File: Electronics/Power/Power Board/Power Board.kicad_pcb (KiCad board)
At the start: 2 copper layers, 117 parts, among them IC201 INA219AIDR, IC202 INA219AIDR, IC203 MP28167GQ-A-Z, IC204 TPS563202DRLR, IC206 TPS563202DRLR, IC301 STM32U575VGT6, IC302 TJA1057GT/3, J201 Conn_01x02_Pin, J202 XT60PW-M, J203 Screw_Terminal_01x02, J204 Screw_Terminal_01x02, J205 Conn_01x02_Pin, J206 Screw_Terminal_01x02, J207 Screw_Terminal_01x02, J208 Conn_01x02_Pin, J209 XT60PW-F, J210 Screw_Terminal_01x02, J211 Screw_Terminal_01x02, J212 Conn_01x02_Pin, J301 TC2030, J302 TYPE-C-31-M-12, J303 Screw_Terminal_01x03, SW201 SW_SPDT, SW301 SW_DIP_x02, U301 USBLC6-4SC6-ES, U302 USBLC6-4SC6-ES, X301 25MHz_Clock, X302 32.768kHz_Clock

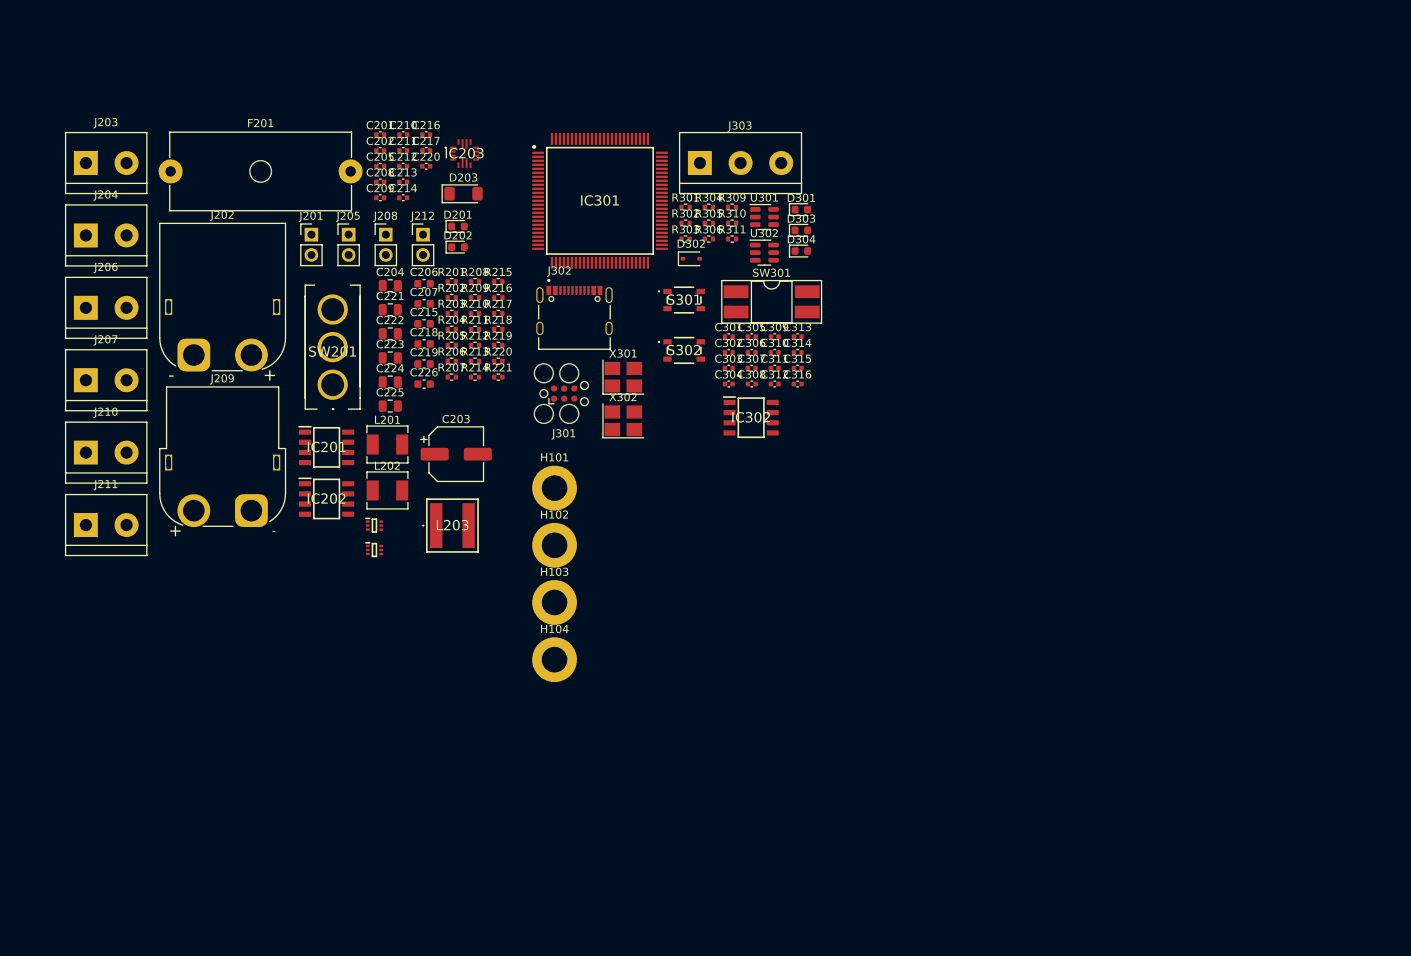
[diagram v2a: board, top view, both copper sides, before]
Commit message: Implemented power supply selector
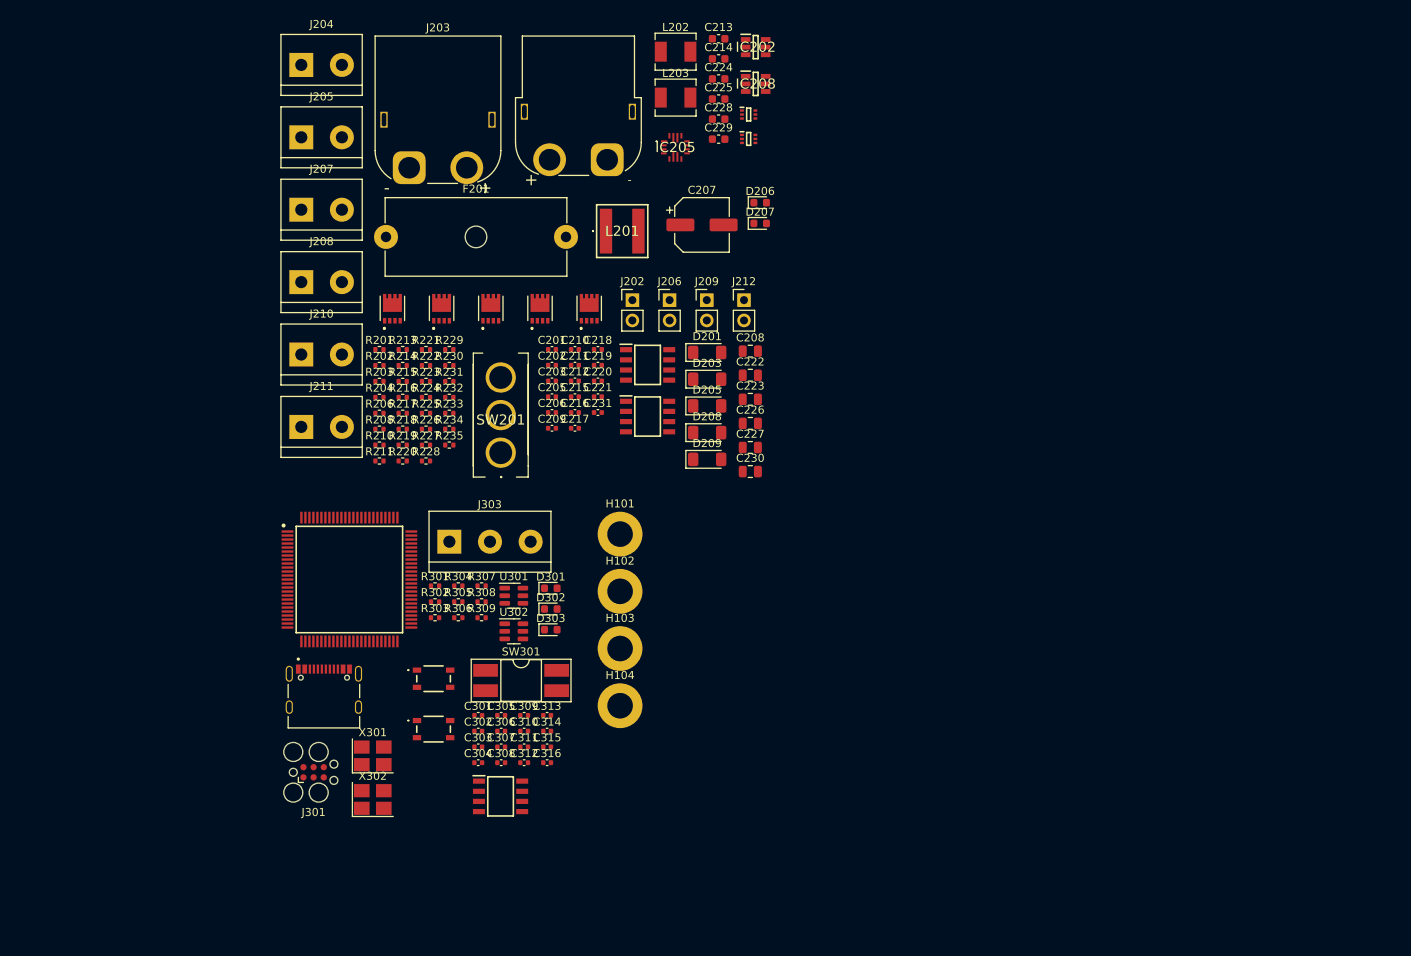
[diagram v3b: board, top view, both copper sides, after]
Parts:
- removed C204: 22u, Capacitor_SMD:C_0805_2012Metric
- removed D202: GREEN, LED_SMD:LED_0603_1608Metric
- removed D304: Blue, LED_SMD:LED_0603_1608Metric
- removed IC203: MP28167GQ-A-Z, MSL Footprints:MP28167GQAZ
- removed R205: 10m, Resistor_SMD:R_0402_1005Metric
- removed R207: 10k, Resistor_SMD:R_0402_1005Metric
- removed R209: 21k5, Resistor_SMD:R_0402_1005Metric
- removed R212: 0R, Resistor_SMD:R_0402_1005Metric
- removed R310, R311: 1k5, Resistor_SMD:R_0402_1005Metric
- added C227: 22u, Capacitor_SMD:C_0805_2012Metric, F.Cu at (194.1, 92.0)
- added C228: 22u, Capacitor_SMD:C_0603_1608Metric, F.Cu at (190.1, 50.9)
- added C229: 22u, Capacitor_SMD:C_0603_1608Metric, F.Cu at (190.1, 53.5)
- added C230: 22u, Capacitor_SMD:C_0805_2012Metric, F.Cu at (194.1, 95.0)
- added C231: 1u, Capacitor_SMD:C_0402_1005Metric, F.Cu at (175.0, 87.6)
- added D205: ZMM10V, Diode_SMD:D_MiniMELF, F.Cu at (188.7, 86.8)
- added D206: GREEN, LED_SMD:LED_0603_1608Metric, F.Cu at (195.3, 61.4)
- added D207: GREEN, LED_SMD:LED_0603_1608Metric, F.Cu at (195.3, 64.0)
- added D208: ZMM16V, Diode_SMD:D_MiniMELF, F.Cu at (188.7, 90.1)
- added D209: ZMM4V7, Diode_SMD:D_MiniMELF, F.Cu at (188.7, 93.5)
- added IC205: MP28167GQ-A-Z, MSL Footprints:MP28167GQAZ, F.Cu at (184.7, 54.5)
- added IC207: TPS563202DRLR, MSL Footprints:SOTFL50P160X60-6N, F.Cu at (193.8, 53.4)
- added IC208: TLV1805DBVR, MSL Footprints:SOT95P280X145-6N, F.Cu at (194.7, 46.5)
- added Q201: DMP3013SFV-7, MSL Footprints:DMP3013SFV7, F.Cu at (149.3, 76.1)
- added Q202: DMP3013SFV-7, MSL Footprints:DMP3013SFV7, F.Cu at (155.5, 76.1)
- added Q203: DMP3013SFV-7, MSL Footprints:DMP3013SFV7, F.Cu at (161.6, 76.1)
- added Q204: DMP3013SFV-7, MSL Footprints:DMP3013SFV7, F.Cu at (167.8, 76.1)
- added Q205: DMP3013SFV-7, MSL Footprints:DMP3013SFV7, F.Cu at (173.9, 76.1)
- added R222: 430k, Resistor_SMD:R_0402_1005Metric, F.Cu at (153.5, 81.7)
- added R223: 39k2, Resistor_SMD:R_0402_1005Metric, F.Cu at (153.5, 83.7)
- added R224: 52k, Resistor_SMD:R_0402_1005Metric, F.Cu at (153.5, 85.7)
- added R225: 10k, Resistor_SMD:R_0402_1005Metric, F.Cu at (153.5, 87.7)
- added R226: 31k, Resistor_SMD:R_0402_1005Metric, F.Cu at (153.5, 89.7)
- added R227: 10k, Resistor_SMD:R_0402_1005Metric, F.Cu at (153.5, 91.7)
- added R228: 2k2, Resistor_SMD:R_0402_1005Metric, F.Cu at (153.5, 93.7)
- added R229: 1k5, Resistor_SMD:R_0402_1005Metric, F.Cu at (156.4, 79.8)
- added R230: 10k, Resistor_SMD:R_0402_1005Metric, F.Cu at (156.4, 81.7)
- added R231: 4k7, Resistor_SMD:R_0402_1005Metric, F.Cu at (156.4, 83.7)
- added R232: 1k, Resistor_SMD:R_0402_1005Metric, F.Cu at (156.4, 85.7)
- added R233: 10k, Resistor_SMD:R_0402_1005Metric, F.Cu at (156.4, 87.7)
- added R234: 100k, Resistor_SMD:R_0402_1005Metric, F.Cu at (156.4, 89.7)
- added R235: 22R, Resistor_SMD:R_0402_1005Metric, F.Cu at (156.4, 91.7)
- added R307: 1k5, Resistor_SMD:R_0402_1005Metric, F.Cu at (160.5, 109.3)
- added R308: 1k5, Resistor_SMD:R_0402_1005Metric, F.Cu at (160.5, 111.3)
- C203: value 100u -> 1u; footprint Capacitor_SMD:CP_Elec_6.3x7.7 -> Capacitor_SMD:C_0402_1005Metric
- C206, C215, C218, C219: value 22u -> 100n; footprint Capacitor_SMD:C_0603_1608Metric -> Capacitor_SMD:C_0402_1005Metric
- C207: value 22u -> 100u; footprint Capacitor_SMD:C_0603_1608Metric -> Capacitor_SMD:CP_Elec_6.3x7.7
- C208: value 100n -> 22u; footprint Capacitor_SMD:C_0402_1005Metric -> Capacitor_SMD:C_0805_2012Metric
- C213, C214: value 100n -> 22u; footprint Capacitor_SMD:C_0402_1005Metric -> Capacitor_SMD:C_0603_1608Metric
- C221: value 22u -> 100n; footprint Capacitor_SMD:C_0805_2012Metric -> Capacitor_SMD:C_0402_1005Metric
- C224, C225: footprint Capacitor_SMD:C_0805_2012Metric -> Capacitor_SMD:C_0603_1608Metric
- C226: footprint Capacitor_SMD:C_0603_1608Metric -> Capacitor_SMD:C_0805_2012Metric
- D201: value GREEN -> ZMM16V; footprint LED_SMD:LED_0603_1608Metric -> Diode_SMD:D_MiniMELF
- D203: value ZMM10V -> ZMM4V7
- D302: value BAT760-115 -> Green; footprint Diode_SMD:D_SOD-323 -> LED_SMD:LED_0603_1608Metric
- D303: value Green -> Blue
- IC202: value INA219AIDR -> TLV1805DBVR; footprint MSL Footprints:SOIC127P600X175-8N -> MSL Footprints:SOT95P280X145-6N
- IC204: value TPS563202DRLR -> INA219AIDR; footprint MSL Footprints:SOTFL50P160X60-6N -> MSL Footprints:SOIC127P600X175-8N
- J201: value Conn_01x02_Pin -> XT60PW-F; footprint Connector_PinHeader_2.54mm:PinHeader_1x02_P2.54mm_Vertical -> MSL Footprints:AMASS_XT60PW-F_1x02_P7.20mm_Horizontal
- J202: value XT60PW-M -> Conn_01x02_Pin; footprint Connector_AMASS:AMASS_XT60PW-M_1x02_P7.20mm_Horizontal -> Connector_PinHeader_2.54mm:PinHeader_1x02_P2.54mm_Vertical
- J203: value Screw_Terminal_01x02 -> XT60PW-M; footprint TerminalBlock:TerminalBlock_bornier-2_P5.08mm -> MSL Footprints:AMASS_XT60PW-M_1x02_P7.20mm_Horizontal
- J205, J208: value Conn_01x02_Pin -> Screw_Terminal_01x02; footprint Connector_PinHeader_2.54mm:PinHeader_1x02_P2.54mm_Vertical -> TerminalBlock:TerminalBlock_bornier-2_P5.08mm
- J206: value Screw_Terminal_01x02 -> Conn_01x02_Pin; footprint TerminalBlock:TerminalBlock_bornier-2_P5.08mm -> Connector_PinHeader_2.54mm:PinHeader_1x02_P2.54mm_Vertical
- J209: value XT60PW-F -> Conn_01x02_Pin; footprint Connector_AMASS:AMASS_XT60PW-F_1x02_P7.20mm_Horizontal -> Connector_PinHeader_2.54mm:PinHeader_1x02_P2.54mm_Vertical
- L201: value 4u7 -> MPL-AL6050-4R7; footprint Inductor_SMD:L_Chilisin_BMRA00040420 -> MSL Footprints:MPLAL60504R7
- L202: value 3u3 -> 4u7
- L203: value MPL-AL6050-4R7 -> 3u3; footprint MSL Footprints:MPLAL60504R7 -> Inductor_SMD:L_Chilisin_BMRA00040420
- R204: value 22R -> 4k7
- R206: value 22R -> 1k
- R210: value 787k -> 330R
- R211: value 0R -> 22R
- R213: value 430k -> 22R
- R214: value 39k2 -> 10m
- R215: value 52k -> 22R
- R217: value 31k -> 100k
- R218: value 10k -> 21k5
- R219: value 2k2 -> 787k
- R220: value 1k5 -> 0R
- R221: value 330R -> 0R
- moved IC202 77.9 mm to (194.7, 41.9)
- moved J206 73.0 mm to (184.0, 73.6)
- moved IC206 71.8 mm to (193.8, 50.4)
- moved L202 65.6 mm to (184.7, 42.5)
- moved J209 62.7 mm to (188.6, 73.6)
- moved L203 60.3 mm to (184.7, 48.3)
- moved R309 60.1 mm to (160.5, 113.3)
- moved D303 58.9 mm to (169.1, 114.8)
- moved C301 56.8 mm to (160.0, 125.5)
- moved C302 56.8 mm to (160.0, 127.5)
- moved R301 56.8 mm to (154.6, 109.3)
- moved R302 56.8 mm to (154.6, 111.3)
- moved C303 56.8 mm to (160.0, 129.4)
- moved C305 56.8 mm to (162.9, 125.5)
- moved C306 56.8 mm to (162.9, 127.5)
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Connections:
- net Net-(SW201-B) renamed /Power/VBAT_FUSED
- C202 pad 1: /Power/BAT_VIN+ -> GND
- C202 pad 2: /Power/BAT_VIN- -> +3V3
- C203 pad 1: VBAT -> /Power/VBAT_SOURCE
- C205 pad 1: GND -> /Power/VDD_VIN+
- C205 pad 2: VBAT -> /Power/VDD_VIN-
- C206 pad 1: VBAT -> GND
- C206 pad 2: GND -> +3V3
- C207 pad 1: +5V -> VDD
- C208 pad 1: VBAT -> VDD
- C209 pad 1: +5V -> GND
- C209 pad 2: GND -> VDD
- C210 pad 2: /Power/12V_EN -> 12V_EN
- C213 pad 1: /Power/5V_BST -> VDD
- C213 pad 2: /Power/5V_SW -> GND
- C214 pad 1: /Power/3V3_BST -> VDD
- C214 pad 2: /Power/3V3_SW -> GND
- C215 pad 1: +5V -> VDD
- C216 pad 1: /Power/12V_SW1 -> VDD
- C216 pad 2: /Power/BST12 -> GND
- C217 pad 1: /Power/BST22 -> /Power/12V_SW1
- C217 pad 2: /Power/12V_SW2 -> /Power/BST12
- C218 pad 1: +3.3V -> /Power/BST22
- C218 pad 2: GND -> /Power/12V_SW2
- C219 pad 1: +5V -> /Power/5V_BST
- C219 pad 2: GND -> /Power/5V_SW
- C220 pad 1: +12V -> /Power/3V3_BST
- C220 pad 2: GND -> /Power/3V3_SW
- C224 pad 1: +12V -> +5V
- C225 pad 1: +12V -> +3.3V
- C226 pad 1: +3.3V -> +12V
- D201 pad 1: /Power/5V_LED_K -> VBAT
- D201 pad 2: +5V -> /Power/VBAT_SHDN_A
- D203 pad 1: /Power/RP_PMOS_S -> /Power/VBAT_SHDN_K
- D203 pad 2: /Power/RP_PMOS_G -> GND
- D302 pad 1: +5V -> /Control/LEDG_K
- D302 pad 2: VBUS -> LEDG
- D303 pad 1: /Control/LEDG_K -> /Control/LEDB_K
- D303 pad 2: LEDG -> LEDB
- IC201 pad 2: GND -> +3V3
- IC202 pad 1: GND -> /Power/VBAT_COMP_OUT
- IC202 pad 2: +3V3 -> GND
- IC202 pad 3: SDA -> /Power/VBAT_COMP-
- IC202 pad 4: SCL -> /Power/VBAT_SOURCE
- IC202 pad 5: +3V3 -> /Power/VBAT_SHDN_K
- IC202 pad 6: GND -> /Power/VBAT_SOURCE
- IC204 pad 1: +5V -> GND
- IC204 pad 2: /Power/3V3_SW -> GND
- IC204 pad 3: GND -> SDA
- IC204 pad 4: /Power/3V3_BST -> SCL
- IC204 pad 5: +5V -> +3V3
- IC204 pad 6: /Power/3V3_FB -> GND
- IC206 pad 1: VBAT -> VDD
- IC206 pad 5: VBAT -> VDD
- J201 pad 1: +5V -> GND
- J201 pad 2: GND -> /Power/12V_OUT
- J202 pad 1: VBAT_RAW -> +5V
- J203 pad 1: VBAT -> GND
- J203 pad 2: GND -> VBAT_RAW
- J204 pad 1: VBAT -> VDD
- J205 pad 1: +5V -> VDD
- J206 pad 1: VBAT -> +5V
- J207 pad 1: VBAT -> VDD
- J208 pad 1: +5V -> VDD
- J209 pad 1: GND -> +5V
- J209 pad 2: /Power/12V_OUT -> GND
- J210 pad 1: VBAT -> VDD
- J211 pad 1: VBAT -> VDD
- L201 pad 1: /Power/5V_SW -> /Power/12V_SW1
- L201 pad 2: +5V -> /Power/12V_SW2
- L202 pad 1: /Power/3V3_SW -> /Power/5V_SW
- L202 pad 2: +3.3V -> +5V
- L203 pad 1: /Power/12V_SW1 -> /Power/3V3_SW
- L203 pad 2: /Power/12V_SW2 -> +3.3V
- R204 pad 1: /Power/RP_PMOS_S -> /Power/VBAT_SHDN_A
- R204 pad 2: /Power/BAT_VIN+ -> GND
- R206 pad 1: VBAT -> /Power/VBAT_SHDN_A
- R206 pad 2: /Power/BAT_VIN- -> /Power/VBAT_SHDN_K
- R208 pad 1: VBAT -> /Power/VBAT_SOURCE
- R208 pad 2: /Power/12V_EN -> /Power/VBAT_GATE
- R210 pad 1: /Power/12V_FB -> /Power/RP_PMOS_G
- R210 pad 2: /Power/12V_FB_MID -> GND
- R211 pad 1: /Power/BST11 -> /Power/VBAT_COMP_OUT
- R211 pad 2: /Power/BST12 -> /Power/VBAT_GATE
- R213 pad 1: +12V -> VIN
- R213 pad 2: /Power/12V_FB_MID -> /Power/VDD_VIN+
- R214 pad 1: /Power/12V_FB_MID -> VDD
- R214 pad 2: GND -> VIN
- R215 pad 1: +5V -> VDD
- R215 pad 2: /Power/5V_FB -> /Power/VDD_VIN-
- R216 pad 1: /Power/5V_FB -> +3.3V
- R216 pad 2: GND -> ALT
- R217 pad 1: +3.3V -> VDD
- R217 pad 2: /Power/3V3_FB -> 12V_EN
- R218 pad 1: /Power/3V3_FB -> /Power/OC
- R219 pad 1: /Power/5V_LED_K -> /Power/12V_FB
- R219 pad 2: GND -> /Power/12V_FB_MID
- R220 pad 1: /Power/3V3_LED_K -> /Power/BST11
- R220 pad 2: GND -> /Power/BST12
- R221 pad 1: /Power/RP_PMOS_G -> /Power/BST22
- R221 pad 2: GND -> /Power/BST21
- R309 pad 2: /Control/LEDR_K -> /Control/LEDB_K
- SW201 pad 1: /Power/RP_PMOS_D -> /Power/VBAT_SWITCHED
- U302 pad 5: VBUS -> +3V3

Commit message: Finished power board layout
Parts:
- removed J205: Screw_Terminal_01x02, TerminalBlock:TerminalBlock_bornier-2_P5.08mm
- removed J212: Conn_01x02_Pin, Connector_PinHeader_2.54mm:PinHeader_1x02_P2.54mm_Vertical
- removed U301: USBLC6-4SC6-ES, Package_TO_SOT_SMD:SOT-23-6
- added C204: 120p, Capacitor_SMD:C_0402_1005Metric, F.Cu at (140.2, 92.3)
- added C233: 120p, Capacitor_SMD:C_0402_1005Metric, F.Cu at (151.8, 67.7)
- added C235: 100n, Capacitor_SMD:C_0402_1005Metric, F.Cu at (128.8, 88.5)
- added C236: 100n, Capacitor_SMD:C_0402_1005Metric, F.Cu at (128.8, 91.0)
- added C237: 1u, Capacitor_SMD:C_0402_1005Metric, F.Cu at (143.8, 64.5)
- added C238: 1u, Capacitor_SMD:C_0402_1005Metric, F.Cu at (132.8, 88.5)
- added D204: BAT760-115, Diode_SMD:D_SOD-323, F.Cu at (141.2, 63.3)
- added D210: BAT760-115, Diode_SMD:D_SOD-323, F.Cu at (131.5, 91.0)
- added IC203: INA219AIDR, MSL Footprints:SOIC127P600X175-8N, F.Cu at (124.2, 89.8)
- added J213: Screw_Terminal_01x02, TerminalBlock:TerminalBlock_bornier-2_P5.08mm, F.Cu at (114.5, 60.0)
- added J214: Screw_Terminal_01x02, TerminalBlock:TerminalBlock_bornier-2_P5.08mm, F.Cu at (114.5, 96.0)
- added J215: Screw_Terminal_01x02, TerminalBlock:TerminalBlock_bornier-2_P5.08mm, F.Cu at (131.5, 54.0)
- added Q206: SSM6K513NU,LF, MSL Footprints:SSM6K513NULF, F.Cu at (135.3, 89.5)
- added Q207: SSM6K513NU,LF, MSL Footprints:SSM6K513NULF, F.Cu at (146.6, 65.0)
- added R205: 33k, Resistor_SMD:R_0402_1005Metric, F.Cu at (138.2, 92.3)
- added R207: 100k, Resistor_SMD:R_0402_1005Metric, F.Cu at (142.0, 90.6)
- added R209: 100k, Resistor_SMD:R_0402_1005Metric, F.Cu at (151.8, 68.8)
- added R212: 33k, Resistor_SMD:R_0402_1005Metric, F.Cu at (149.8, 67.7)
- added R236: 22R, Resistor_SMD:R_0402_1005Metric, F.Cu at (130.2, 88.0)
- added R237: 10m, Resistor_SMD:R_0402_1005Metric, F.Cu at (131.8, 88.5)
- added R238: 22R, Resistor_SMD:R_0402_1005Metric, F.Cu at (130.2, 89.0)
- added R310: 10k, Resistor_SMD:R_0402_1005Metric, F.Cu at (195.2, 113.2)
- added R311: 1k, Resistor_SMD:R_0402_1005Metric, F.Cu at (195.2, 115.2)
- added R312: 10k, Resistor_SMD:R_0402_1005Metric, F.Cu at (195.2, 117.2)
- added R313: 1k, Resistor_SMD:R_0402_1005Metric, F.Cu at (195.2, 119.2)
- added U201: TCKE800NA_RF, MSL Footprints:WSON10B_TOS, F.Cu at (139.2, 89.5)
- added U202: TCKE812NA_RF, MSL Footprints:WSON10B_TOS, F.Cu at (150.8, 65.0)
- added U203: TVS1800DRV, Package_SON:WSON-6-1EP_2x2mm_P0.65mm_EP1x1.6mm, F.Cu at (171.4, 105.7)
- added U303: TVS1800DRV, Package_SON:WSON-6-1EP_2x2mm_P0.65mm_EP1x1.6mm, F.Cu at (164.9, 112.6)
- moved H101 81.7 mm to (113.0, 53.0)
- moved IC208 80.8 mm to (156.5, 117.7), turned to 90 degrees
- moved IC202 75.0 mm to (156.5, 106.5), turned to 90 degrees
- moved H102 68.4 mm to (113.0, 132.0)
- moved C225 66.4 mm to (133.5, 83.2)
- moved J209 65.8 mm to (123.2, 81.0), turned to 90 degrees
- moved C214 64.5 mm to (139.5, 83.5), turned to -90 degrees
- moved IC207 64.4 mm to (136.2, 82.2), turned to -90 degrees
- moved H103 64.4 mm to (172.0, 53.0)
- moved C229 63.3 mm to (133.5, 81.8)
- moved C224 62.0 mm to (133.8, 71.8)
- moved IC206 61.4 mm to (136.5, 72.2), turned to -90 degrees
- moved J206 60.7 mm to (123.2, 73.5), turned to 90 degrees
- moved C228 60.6 mm to (133.8, 73.2)
- moved C213 60.0 mm to (139.8, 73.5), turned to -90 degrees
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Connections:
- D208 pad 1: VBAT -> VBUS
- IC301 pad 52: unconnected-(IC301-PB13-Pad52) -> SCL
- IC301 pad 53: unconnected-(IC301-PB14-Pad53) -> SDA
- IC301 pad 92: SCL -> unconnected-(IC301-PB6-Pad92)
- IC301 pad 93: SDA -> unconnected-(IC301-PB7-Pad93)
- J204 pad 1: VDD -> VBAT_RAW
- J207 pad 1: VDD -> VOUT
- J208 pad 1: VDD -> VOUT
- J210 pad 1: VDD -> VOUT
- J211 pad 1: VDD -> VOUT
- Q202 pad 5: VBAT -> VBUS
- Q202 pad 6: VBAT -> VBUS
- Q202 pad 7: VBAT -> VBUS
- Q202 pad 8: VBAT -> VBUS
- Q202 pad 9: VBAT -> VBUS
- R201 pad 1: +12V -> /Power/12V_OUT_D
- R202 pad 2: +12V -> /Power/12V_OUT_D
- R233 pad 1: VBAT -> VBUS
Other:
- board outline added: 65 x 85 mm
- copper layers 2 -> 4
- board text added: "3.3V"
- board text added: "5.0V"
